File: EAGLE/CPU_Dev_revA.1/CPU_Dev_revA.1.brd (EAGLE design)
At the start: 50.8 x 38.1 mm, 29 parts, among them J1 MICRO_USB_SMD, J2 HEADER_5PIN, J3 HEADER_2PIN, J4 HEADER_16PIN, J5 HEADER_16PIN, J6 HEADER_3PIN, SW1 RESET, U1 STM32L151C8T6, U2 3.3V LDO, Y1 16MHz

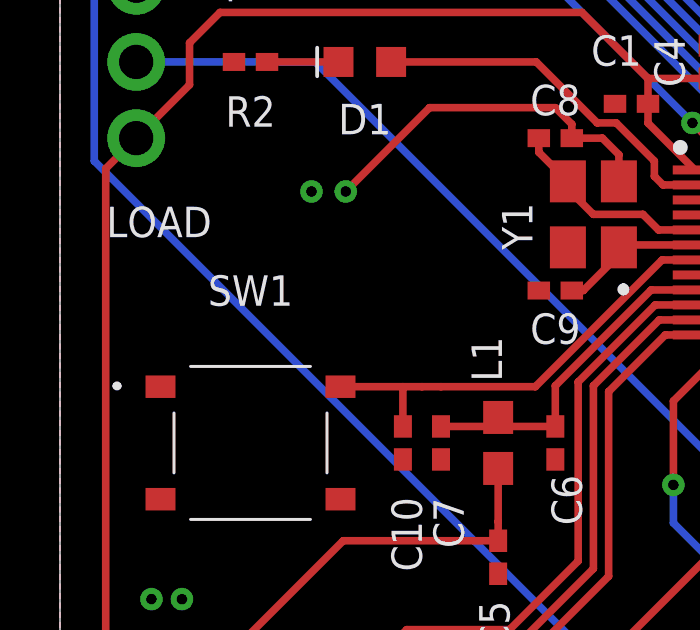
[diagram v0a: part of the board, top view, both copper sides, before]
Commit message: LoRa Silkscreen
Silkscreen and gerber files added
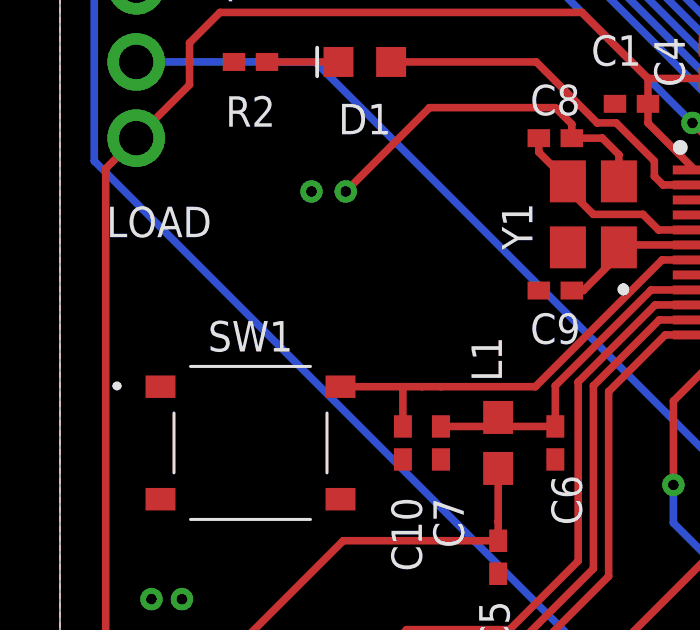
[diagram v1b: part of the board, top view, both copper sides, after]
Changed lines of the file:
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@@
 <drawing>
 <settings>
-<setting alwaysvectorfont="yes"/>
+<setting alwaysvectorfont="no"/>
 <setting verticaltext="up"/>
 </settings>
@@
 </element>
 <element name="SW1" library="NSE LABS" package="PUSHBUTTON_SMD" value="RESET" x="6.35" y="12.7" smashed="yes">
-<attribute name="NAME" x="6.35" y="17.78" size="1.016" layer="25" font="vector" align="center"/>
+<attribute name="NAME" x="6.35" y="16.256" size="1.016" layer="25" font="vector" align="center"/>
 <attribute name="VALUE" x="6.35" y="7.62" size="1.27" layer="27" align="center"/>
 </element>

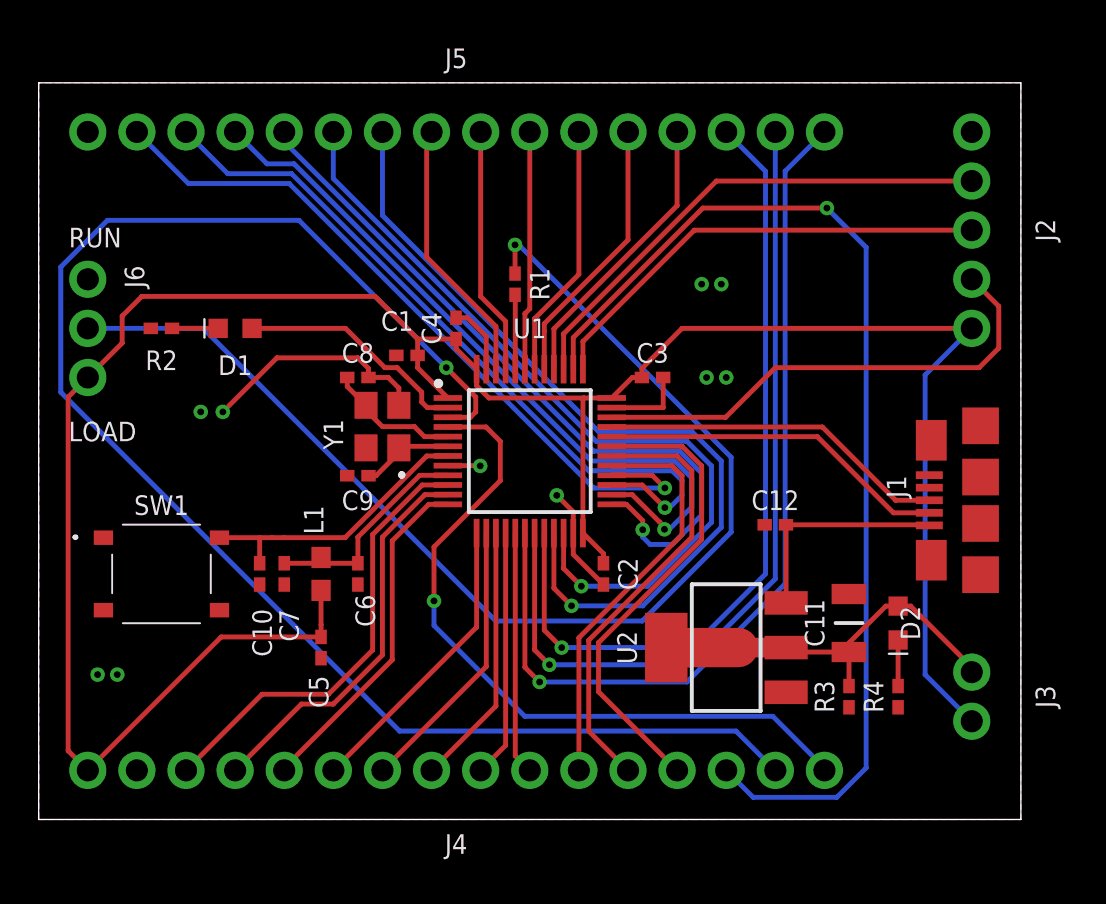
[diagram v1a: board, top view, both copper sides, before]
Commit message: Gerber and Fab Files created
silkscreen and origin modified
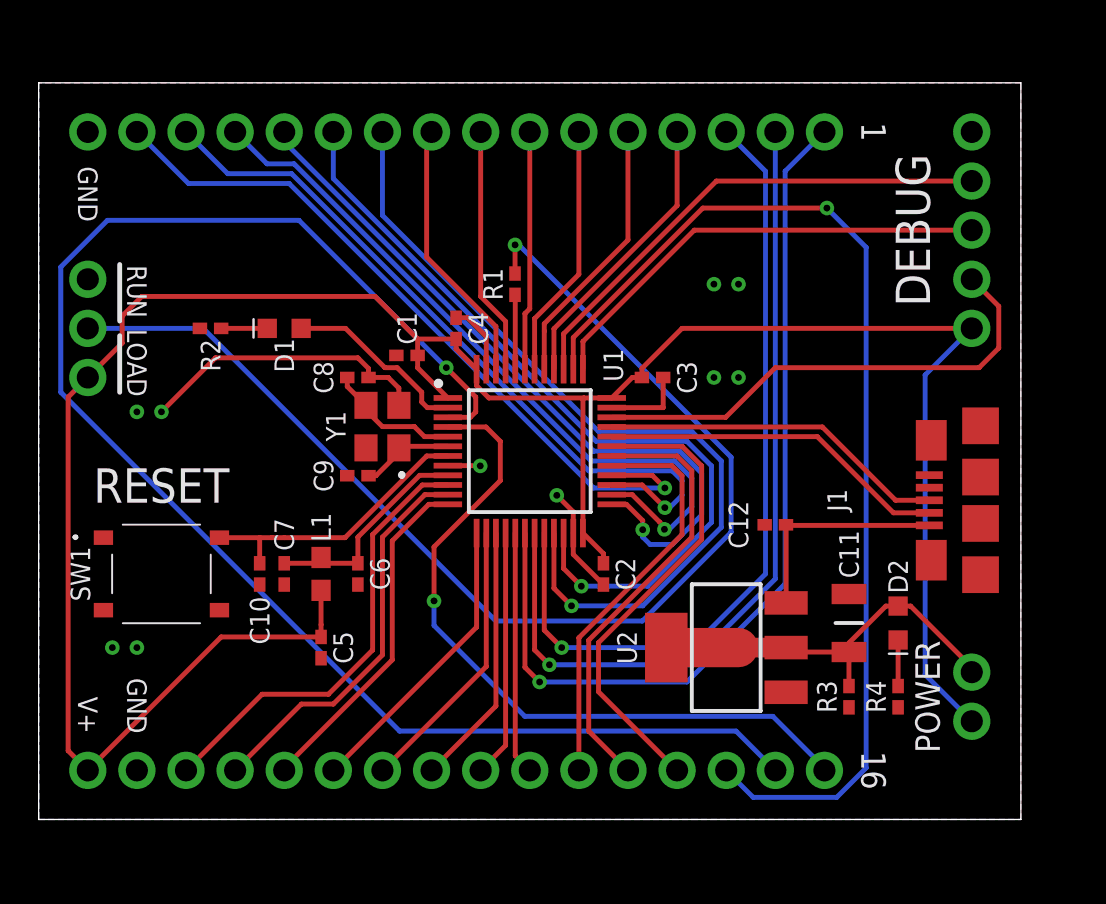
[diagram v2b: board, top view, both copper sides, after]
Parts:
- moved J1 2.90 mm to (47.3, 16.5)
- moved R2 2.54 mm to (8.89, 25.4)
- moved D1 2.54 mm to (12.7, 25.4)
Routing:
- net GND: track 27.3 -> 30.4 mm
- net WKUP: track 12.1 -> 9.58 mm
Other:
- board text added: "1"
- board text added: "16"
- board text added: "CPU DEVELOPMENT BOARD revA.1"
- board text added: "DEBUG"
- board text added: "GND"
- board text added: "NSE LABS"
- board text added: "POWER"
- board text added: "RESET"
- board text added: "V+"
